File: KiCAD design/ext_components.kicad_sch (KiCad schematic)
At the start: 5 parts

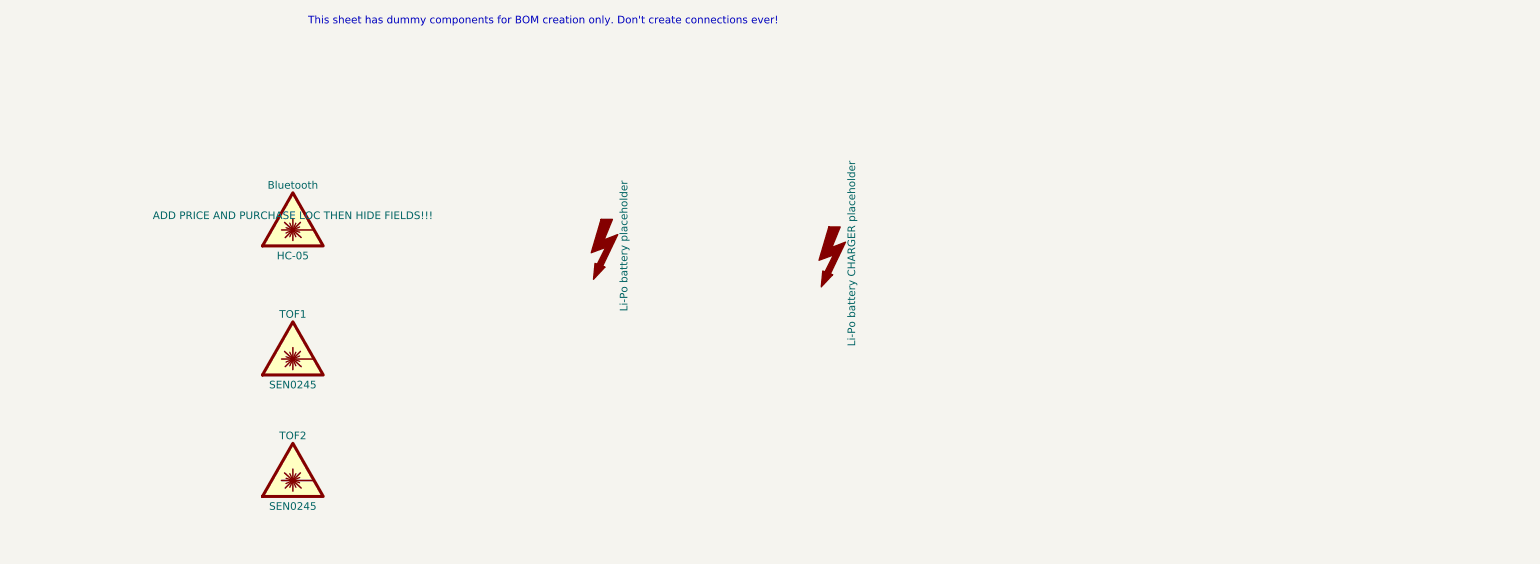
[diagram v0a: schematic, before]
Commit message: add some comments, connector for battery, bluetooth (is now the PMOD BLE from digikey)
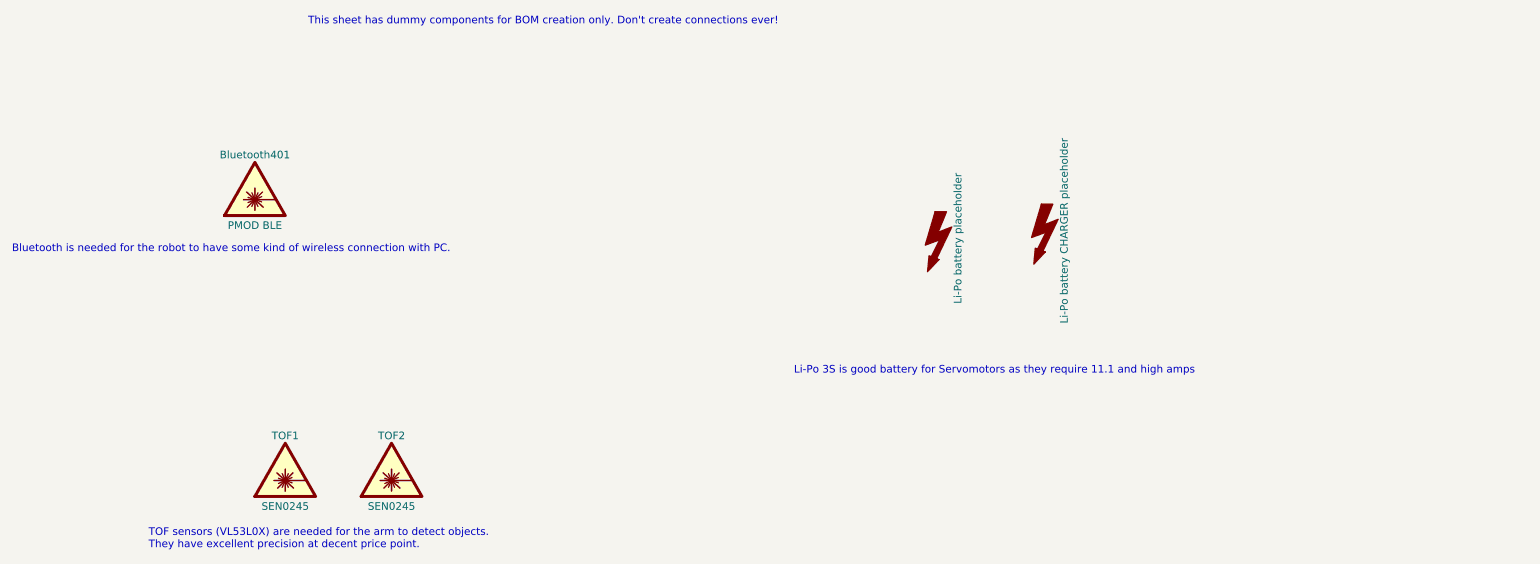
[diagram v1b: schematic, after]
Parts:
- Bluetooth401: renamed from Bluetooth; value HC-05 -> PMOD BLE; Price (none) -> 23.38; PurchaseLoc ADD PRICE AND PURCHASE LOC THEN HIDE FIELDS!!! -> https://www.digikey.fi/en/products/detail/digilent-inc/410-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
- gave numbers to parts that had none: 2
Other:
- note added: "Bluetooth is needed for the robot to have some kind of wireless connection with PC."
- note added: "Li-Po 3S is good battery for Servomotors as they require 11.1 and high amps"
- note added: "TOF sensors (VL53L0X) are needed for the arm to detect objects. They have excellent precision at decent price point."
- moved on the sheet: Bluetooth401, TOF1, TOF2
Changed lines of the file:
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@@
 (kicad_sch (version 20211123) (generator eeschema)
   (paper "A4")
+  (text "Bluetooth is needed for the robot to have some kind of wireless connection with PC."
+    (at 48.26 100.33 0)
+    (effects (font (size 1.27 1.27)) (justify left bottom))
+  )
   (text "This sheet has dummy components for BOM creation only. Don't create connections ever!"
     (at 97.79 62.23 0)
     (effects (font (size 1.27 1.27)) (justify left bottom))
   )
-  (symbol (lib_id "Graphic:SYM_Flash_Large") (at 147.32 99.06 0) (unit 1)
+  (text "TOF sensors (VL53L0X) are needed for the arm to detect objects.\nThey have excellent precision at decent price point."
+    (at 71.12 149.86 0)
+    (effects (font (size 1.27 1.27)) (justify left bottom))
+  )
+  (text "Li-Po 3S is good battery for Servomotors as they require 11.1 and high amps"
+    (at 179.07 120.65 0)
+    (effects (font (size 1.27 1.27)) (justify left bottom))
+  )
+  (symbol (lib_id "Graphic:SYM_Flash_Large") (at 203.2 97.79 0) (unit 1)
     (in_bom yes) (on_board yes) (fields_autoplaced)
-    (property "Reference" "LiPo_bat?" (id 0) (at 143.51 99.06 90)
+    (property "Reference" "LiPo_bat401" (id 0) (at 199.39 97.79 90)
       (effects (font (size 1.27 1.27)) hide)
     )
-    (property "Value" "Li-Po battery placeholder" (id 1) (at 150.622 99.06 90))
-    (property "Footprint" "" (id 2) (at 147.066 101.346 0)
+    (property "Value" "Li-Po battery placeholder" (id 1) (at 206.502 97.79 90))
+    (property "Footprint" "" (id 2) (at 202.946 100.076 0)
       (effects (font (size 1.27 1.27)) hide)
     )
-    (property "Datasheet" "~" (id 3) (at 157.48 101.6 0)
+    (property "Datasheet" "~" (id 3) (at 213.36 100.33 0)
       (effects (font (size 1.27 1.27)) hide)
     )
-    (property "PurchaseLoc" "https://hobbyking.com/en_us/zippy-compact-1800mah-3s-25c-lipo-pack.html" (id 4) (at 147.32 99.06 90)
+    (property "PurchaseLoc" "https://hobbyking.com/en_us/zippy-compact-1800mah-3s-25c-lipo-pack.html" (id 4) (at 203.2 97.79 90)
       (effects (font (size 1.27 1.27)) hide)
     )
-    (property "Price" "13.42" (id 5) (at 147.32 99.06 90)
+    (property "Price" "13.42" (id 5) (at 203.2 97.79 90)
       (effects (font (size 1.27 1.27)) hide)
     )
   )
-  (symbol (lib_id "Graphic:SYM_Flash_Large") (at 185.42 100.33 0) (unit 1)
+  (symbol (lib_id "Graphic:SYM_Flash_Large") (at 220.98 96.52 0) (unit 1)
     (in_bom yes) (on_board yes) (fields_autoplaced)
-    (property "Reference" "LiPo_charger?" (id 0) (at 181.61 100.33 90)
+    (property "Reference" "LiPo_charger401" (id 0) (at 217.17 96.52 90)
       (effects (font (size 1.27 1.27)) hide)
     )
-    (property "Value" "Li-Po battery CHARGER placeholder" (id 1) (at 188.722 100.33 90))
-    (property "Footprint" "" (id 2) (at 185.166 102.616 0)
+    (property "Value" "Li-Po battery CHARGER placeholder" (id 1) (at 224.282 96.52 90))
+    (property "Footprint" "" (id 2) (at 220.726 98.806 0)
       (effects (font (size 1.27 1.27)) hide)
     )
-    (property "Datasheet" "~" (id 3) (at 195.58 102.87 0)
+    (property "Datasheet" "~" (id 3) (at 231.14 99.06 0)
       (effects (font (size 1.27 1.27)) hide)
     )
-    (property "PurchaseLoc" "https://hobbyking.com/en_us/turnigy-e3-compact-2s-3s-lipo-charger-100-240v-eu-plug.html" (id 4) (at 185.42 100.33 90)
+    (property "PurchaseLoc" "https://hobbyking.com/en_us/turnigy-e3-compact-2s-3s-lipo-charger-100-240v-eu-plug.html" (id 4) (at 220.98 96.52 90)
       (effects (font (size 1.27 1.27)) hide)
     )
-    (property "Price" "14.39" (id 5) (at 185.42 100.33 90)
+    (property "Price" "14.39" (id 5) (at 220.98 96.52 90)
       (effects (font (size 1.27 1.27)) hide)
     )
   )
-  (symbol (lib_id "Graphic:SYM_LASER_Large") (at 95.25 115.57 0) (unit 1)
+  (symbol (lib_id "Graphic:SYM_LASER_Large") (at 93.98 135.89 0) (unit 1)
     (in_bom yes) (on_board yes) (fields_autoplaced)
-    (property "Reference" "TOF1" (id 0) (at 95.25 110.49 0))
-    (property "Value" "SEN0245" (id 1) (at 95.25 122.301 0))
-    (property "Footprint" "" (id 2) (at 94.996 120.015 0)
+    (property "Reference" "TOF1" (id 0) (at 93.98 130.81 0))
+    (property "Value" "SEN0245" (id 1) (at 93.98 142.621 0))
+    (property "Footprint" "" (id 2) (at 93.726 140.335 0)
       (effects (font (size 1.27 1.27)) hide)
     )
-    (property "Datasheet" "~" (id 3) (at 96.012 120.65 0)
+    (property "Datasheet" "~" (id 3) (at 94.742 140.97 0)
       (effects (font (size 1.27 1.27)) hide)
     )
-    (property "PurchaseLoc" "https://www.digikey.fi/en/products/detail/dfrobot/SEN0245/8827827?s=N4IgTCBcDaIG4BsCsBmBAGAHiAugXyA" (id 4) (at 95.25 115.57 0)
+    (property "PurchaseLoc" "https://www.digikey.fi/en/products/detail/dfrobot/SEN0245/8827827?s=N4IgTCBcDaIG4BsCsBmBAGAHiAugXyA" (id 4) (at 93.98 135.89 0)
       (effects (font (size 1.27 1.27)) hide)
     )
-    (property "Price" "12.07" (id 5) (at 95.25 115.57 0)
+    (property "Price" "12.07" (id 5) (at 93.98 135.89 0)
       (effects (font (size 1.27 1.27)) hide)
     )
   )
-  (symbol (lib_id "Graphic:SYM_LASER_Large") (at 95.25 135.89 0) (unit 1)
+  (symbol (lib_id "Graphic:SYM_LASER_Large") (at 111.76 135.89 0) (unit 1)
     (in_bom yes) (on_board yes) (fields_autoplaced)
-    (property "Reference" "TOF2" (id 0) (at 95.25 130.81 0))
-    (property "Value" "SEN0245" (id 1) (at 95.25 142.621 0))
-    (property "Footprint" "" (id 2) (at 94.996 140.335 0)
+    (property "Reference" "TOF2" (id 0) (at 111.76 130.81 0))
+    (property "Value" "SEN0245" (id 1) (at 111.76 142.621 0))
+    (property "Footprint" "" (id 2) (at 111.506 140.335 0)
       (effects (font (size 1.27 1.27)) hide)
     )
-    (property "Datasheet" "~" (id 3) (at 96.012 140.97 0)
+    (property "Datasheet" "~" (id 3) (at 112.522 140.97 0)
       (effects (font (size 1.27 1.27)) hide)
     )
-    (property "PurchaseLoc" "https://www.digikey.fi/en/products/detail/dfrobot/SEN0245/8827827?s=N4IgTCBcDaIG4BsCsBmBAGAHiAugXyA" (id 4) (at 95.25 135.89 0)
+    (property "PurchaseLoc" "https://www.digikey.fi/en/products/detail/dfrobot/SEN0245/8827827?s=N4IgTCBcDaIG4BsCsBmBAGAHiAugXyA" (id 4) (at 111.76 135.89 0)
       (effects (font (size 1.27 1.27)) hide)
     )
-    (property "Price" "12.07" (id 5) (at 95.25 135.89 0)
+    (property "Price" "12.07" (id 5) (at 111.76 135.89 0)
       (effects (font (size 1.27 1.27)) hide)
     )
   )
-  (symbol (lib_id "Graphic:SYM_LASER_Large") (at 95.25 93.98 0) (unit 1)
+  (symbol (lib_id "Graphic:SYM_LASER_Large") (at 88.9 88.9 0) (unit 1)
     (in_bom yes) (on_board yes) (fields_autoplaced)
-    (property "Reference" "Bluetooth" (id 0) (at 95.25 88.9 0))
-    (property "Value" "HC-05" (id 1) (at 95.25 100.711 0))
-    (property "Footprint" "" (id 2) (at 94.996 98.425 0)
+    (property "Reference" "Bluetooth401" (id 0) (at 88.9 83.82 0))
+    (property "Value" "PMOD BLE" (id 1) (at 88.9 95.631 0))
+    (property "Footprint" "" (id 2) (at 88.646 93.345 0)
       (effects (font (size 1.27 1.27)) hide)
     )
-    (property "Datasheet" "~" (id 3) (at 96.012 99.06 0)
+    (property "Datasheet" "~" (id 3) (at 89.662 93.98 0)
       (effects (font (size 1.27 1.27)) hide)
     )
-    (property "PurchaseLoc" "ADD PRICE AND PURCHASE LOC THEN HIDE FIELDS!!!" (id 4) (at 95.25 93.98 0))
-    (property "Price" "" (id 5) (at 95.25 93.98 0))
+    (property "PurchaseLoc" "https://www.digikey.fi/en/products/detail/digilent-inc/410-359/8605090" (id 4) (at 88.9 88.9 0)
+      (effects (font (size 1.27 1.27)) hide)
+    )
+    (property "Price" "23.38" (id 5) (at 88.9 88.9 0)
+      (effects (font (size 1.27 1.27)) hide)
+    )
   )
 )

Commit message: add link to switch and 1k resistor
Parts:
- TOF1, TOF2: Price 12.07 -> 24.14
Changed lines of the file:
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@@
       (effects (font (size 1.27 1.27)) hide)
     )
-    (property "Price" "12.07" (id 5) (at 93.98 135.89 0)
+    (property "Price" "24.14" (id 5) (at 93.98 135.89 0)
       (effects (font (size 1.27 1.27)) hide)
     )
@@
       (effects (font (size 1.27 1.27)) hide)
     )
-    (property "Price" "12.07" (id 5) (at 111.76 135.89 0)
+    (property "Price" "24.14" (id 5) (at 111.76 135.89 0)
       (effects (font (size 1.27 1.27)) hide)
     )

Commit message: use individual prices
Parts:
- TOF1, TOF2: Price 24.14 -> 12.07
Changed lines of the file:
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@@
       (effects (font (size 1.27 1.27)) hide)
     )
-    (property "Price" "24.14" (id 5) (at 93.98 135.89 0)
+    (property "Price" "12.07" (id 5) (at 93.98 135.89 0)
       (effects (font (size 1.27 1.27)) hide)
     )
@@
       (effects (font (size 1.27 1.27)) hide)
     )
-    (property "Price" "24.14" (id 5) (at 111.76 135.89 0)
+    (property "Price" "12.07" (id 5) (at 111.76 135.89 0)
       (effects (font (size 1.27 1.27)) hide)
     )

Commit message: more comments (no changes in functionality)
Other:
- note added: "Li-Po 3S is good battery for Servomotors as they require 11.1 and high amperage (servomotor stall torque current 1.5 A)."
- note added: "This sheet has dummy components for BOM creation only. Don't create connections here."
- note removed: "Li-Po 3S is good battery for Servomotors as they require 11.1 and high amps"
- note removed: "This sheet has dummy components for BOM creation only. Don't create connections ever!"
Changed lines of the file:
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@@
     (effects (font (size 1.27 1.27)) (justify left bottom))
   )
-  (text "This sheet has dummy components for BOM creation only. Don't create connections ever!"
+  (text "This sheet has dummy components for BOM creation only. Don't create connections here."
     (at 97.79 62.23 0)
     (effects (font (size 1.27 1.27)) (justify left bottom))
@@
     (effects (font (size 1.27 1.27)) (justify left bottom))
   )
-  (text "Li-Po 3S is good battery for Servomotors as they require 11.1 and high amps"
-    (at 179.07 120.65 0)
+  (text "Li-Po 3S is good battery for Servomotors as they require 11.1 and high amperage (servomotor stall torque current 1.5 A)."
+    (at 156.21 120.65 0)
     (effects (font (size 1.27 1.27)) (justify left bottom))
   )

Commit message: tof sensor values and lipo bat
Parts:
- LiPo_bat401: Price 13.42 -> 12.34; PurchaseLoc https://hobbyking.com/en_us/zippy-compact-1800mah-3s-25c-li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 -> https://hobbyking.com/en_us/turnigy-2200mah-3s-25c-lipo-pac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
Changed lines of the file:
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@@
       (effects (font (size 1.27 1.27)) hide)
     )
-    (property "PurchaseLoc" "https://hobbyking.com/en_us/zippy-compact-1800mah-3s-25c-lipo-pack.html" (id 4) (at 203.2 97.79 90)
+    (property "PurchaseLoc" "https://hobbyking.com/en_us/turnigy-2200mah-3s-25c-lipo-pack.html" (id 4) (at 203.2 97.79 90)
       (effects (font (size 1.27 1.27)) hide)
     )
-    (property "Price" "13.42" (id 5) (at 203.2 97.79 90)
+    (property "Price" "12.34" (id 5) (at 203.2 97.79 90)
       (effects (font (size 1.27 1.27)) hide)
     )

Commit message: tof sensor update
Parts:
- TOF1, TOF2: Price 12.07 -> 13.75; PurchaseLoc https://www.digikey.fi/en/products/detail/dfrobot/SEN0245/8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 -> https://www.digikey.fi/en/products/detail/adafruit-industri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
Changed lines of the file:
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@@
       (effects (font (size 1.27 1.27)) hide)
     )
-    (property "PurchaseLoc" "https://www.digikey.fi/en/products/detail/dfrobot/SEN0245/8827827?s=N4IgTCBcDaIG4BsCsBmBAGAHiAugXyA" (id 4) (at 93.98 135.89 0)
+    (property "PurchaseLoc" "https://www.digikey.fi/en/products/detail/adafruit-industries-llc/3317/6569762" (id 4) (at 93.98 135.89 0)
       (effects (font (size 1.27 1.27)) hide)
     )
-    (property "Price" "12.07" (id 5) (at 93.98 135.89 0)
+    (property "Price" "13.75" (id 5) (at 93.98 135.89 0)
       (effects (font (size 1.27 1.27)) hide)
     )
@@
       (effects (font (size 1.27 1.27)) hide)
     )
-    (property "PurchaseLoc" "https://www.digikey.fi/en/products/detail/dfrobot/SEN0245/8827827?s=N4IgTCBcDaIG4BsCsBmBAGAHiAugXyA" (id 4) (at 111.76 135.89 0)
+    (property "PurchaseLoc" "https://www.digikey.fi/en/products/detail/adafruit-industries-llc/3317/6569762" (id 4) (at 111.76 135.89 0)
       (effects (font (size 1.27 1.27)) hide)
     )
-    (property "Price" "12.07" (id 5) (at 111.76 135.89 0)
+    (property "Price" "13.75" (id 5) (at 111.76 135.89 0)
       (effects (font (size 1.27 1.27)) hide)
     )
